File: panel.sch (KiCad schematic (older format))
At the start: 31 parts, among them J201 AudioJack2, J202 AudioJack2, J203 AudioJack2, J204 Conn_01x14, J205 AudioJack2, J206 AudioJack2, J207 Conn_01x09, J208 AudioJack2, J209 AudioJack2, J210 AudioJack2, SW201 SR1712F-0204-20F0A-N9-N-027, U201 TL072

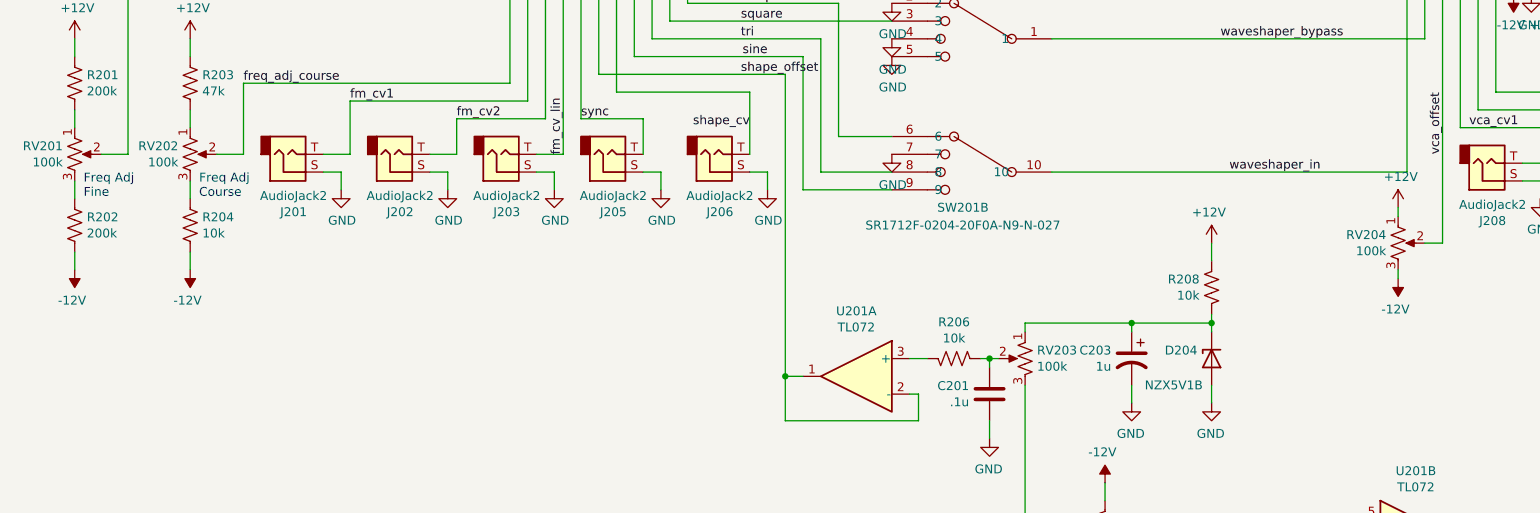
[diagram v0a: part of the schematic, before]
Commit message: Updated for tayda pots A-5513 and jacks A-2563
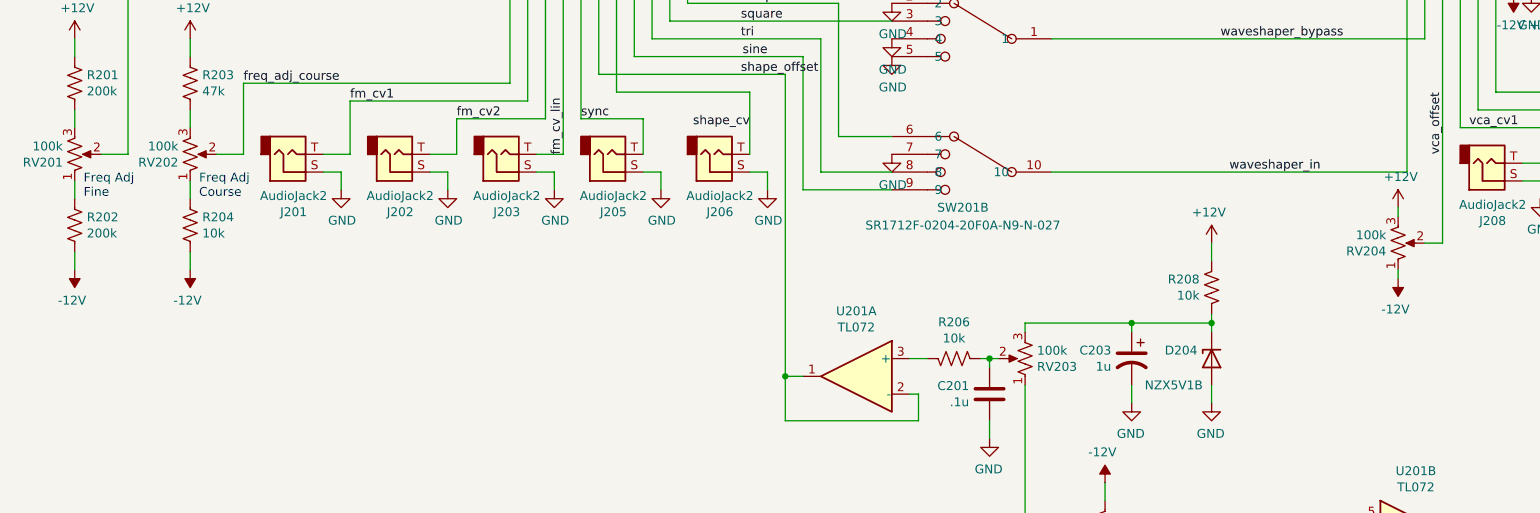
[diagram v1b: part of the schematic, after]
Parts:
- J201, J202, J203, J205, J206, J208, J209, J210: footprint ACJM-MV35:ACJM-MV35 -> A-2563:A-2563
- RV201, RV202, RV203, RV204: footprint Potentiometer_THT:Potentiometer_Bourns_PTV09A-1_Single_Vertical -> A-5513:A-5513
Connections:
- net +12V: now also RV204.3; no longer RV204.1
- net -12V: now also RV204.1; no longer RV204.3
- net at RV201.1: now also R202.1; no longer R201.2
- net at RV201.3: now also R201.2; no longer R202.1
- net at RV202.1: now also R204.1; no longer R203.2
- net at RV202.3: now also R203.2; no longer R204.1
- net at C203.1, D204.1 (K), R208.1: now also RV203.3; no longer RV203.1
- net at C202.2, D203.2 (A), R207.1: now also RV203.1; no longer RV203.3
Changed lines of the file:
@@
 F 0 "RV204" H 8283 3996 50  0000 R CNN
 F 1 "100k" H 8283 3905 50  0000 R CNN
-F 2 "Potentiometer_THT:Potentiometer_Bourns_PTV09A-1_Single_Vertical" H 8350 3950 50  0001 C CNN
+F 2 "A-5513:A-5513" H 8350 3950 50  0001 C CNN
 F 3 "~" H 8350 3950 50  0001 C CNN
 	1    8350 3950
-	1    0    0    -1
+	1    0    0    1
 $EndComp
 Wire Wire Line
@@
 F 0 "RV201" H 833 3496 50  0000 R CNN
 F 1 "100k" H 833 3405 50  0000 R CNN
-F 2 "Potentiometer_THT:Potentiometer_Bourns_PTV09A-1_Single_Vertical" H 900 3450 50  0001 C CNN
+F 2 "A-5513:A-5513" H 900 3450 50  0001 C CNN
 F 3 "~" H 900 3450 50  0001 C CNN
 	1    900  3450
-	1    0    0    -1
+	1    0    0    1
 $EndComp
 $Comp
@@
 F 0 "RV202" H 1483 3496 50  0000 R CNN
 F 1 "100k" H 1483 3405 50  0000 R CNN
-F 2 "Potentiometer_THT:Potentiometer_Bourns_PTV09A-1_Single_Vertical" H 1550 3450 50  0001 C CNN
+F 2 "A-5513:A-5513" H 1550 3450 50  0001 C CNN
 F 3 "~" H 1550 3450 50  0001 C CNN
 	1    1550 3450
-	1    0    0    -1
+	1    0    0    1
 $EndComp
 $Comp
@@
 F 0 "J201" H 2132 3775 50  0000 C CNN
 F 1 "AudioJack2" H 2132 3684 50  0000 C CNN
-F 2 "ACJM-MV35:ACJM-MV35" H 2100 3450 50  0001 C CNN
+F 2 "A-2563:A-2563" H 2100 3450 50  0001 C CNN
 F 3 "~" H 2100 3450 50  0001 C CNN
 	1    2100 3450
@@
 F 0 "J202" H 2732 3775 50  0000 C CNN
 F 1 "AudioJack2" H 2732 3684 50  0000 C CNN
-F 2 "ACJM-MV35:ACJM-MV35" H 2700 3450 50  0001 C CNN
+F 2 "A-2563:A-2563" H 2700 3450 50  0001 C CNN
 F 3 "~" H 2700 3450 50  0001 C CNN
 	1    2700 3450
@@
 F 0 "J203" H 3332 3775 50  0000 C CNN
 F 1 "AudioJack2" H 3332 3684 50  0000 C CNN
-F 2 "ACJM-MV35:ACJM-MV35" H 3300 3450 50  0001 C CNN
+F 2 "A-2563:A-2563" H 3300 3450 50  0001 C CNN
 F 3 "~" H 3300 3450 50  0001 C CNN
 	1    3300 3450
@@
 F 0 "J205" H 3932 3775 50  0000 C CNN
 F 1 "AudioJack2" H 3932 3684 50  0000 C CNN
-F 2 "ACJM-MV35:ACJM-MV35" H 3900 3450 50  0001 C CNN
+F 2 "A-2563:A-2563" H 3900 3450 50  0001 C CNN
 F 3 "~" H 3900 3450 50  0001 C CNN
 	1    3900 3450
@@
 F 0 "J206" H 4532 3775 50  0000 C CNN
 F 1 "AudioJack2" H 4532 3684 50  0000 C CNN
-F 2 "ACJM-MV35:ACJM-MV35" H 4500 3450 50  0001 C CNN
+F 2 "A-2563:A-2563" H 4500 3450 50  0001 C CNN
 F 3 "~" H 4500 3450 50  0001 C CNN
 	1    4500 3450
@@
 F 0 "RV203" H 6183 4646 50  0000 R CNN
 F 1 "100k" H 6183 4555 50  0000 R CNN
-F 2 "Potentiometer_THT:Potentiometer_Bourns_PTV09A-1_Single_Vertical" H 6250 4600 50  0001 C CNN
+F 2 "A-5513:A-5513" H 6250 4600 50  0001 C CNN
 F 3 "~" H 6250 4600 50  0001 C CNN
 	1    6250 4600
-	-1   0    0    -1
+	-1   0    0    1
 $EndComp
 $Comp
@@
 F 0 "J208" H 8882 3825 50  0000 C CNN
 F 1 "AudioJack2" H 8882 3734 50  0000 C CNN
-F 2 "ACJM-MV35:ACJM-MV35" H 8850 3500 50  0001 C CNN
+F 2 "A-2563:A-2563" H 8850 3500 50  0001 C CNN
 F 3 "~" H 8850 3500 50  0001 C CNN
 	1    8850 3500
@@
 F 0 "J209" H 9532 3825 50  0000 C CNN
 F 1 "AudioJack2" H 9532 3734 50  0000 C CNN
-F 2 "ACJM-MV35:ACJM-MV35" H 9500 3500 50  0001 C CNN
+F 2 "A-2563:A-2563" H 9500 3500 50  0001 C CNN
 F 3 "~" H 9500 3500 50  0001 C CNN
 	1    9500 3500
@@
 F 0 "J210" H 10182 3825 50  0000 C CNN
 F 1 "AudioJack2" H 10182 3734 50  0000 C CNN
-F 2 "ACJM-MV35:ACJM-MV35" H 10150 3500 50  0001 C CNN
+F 2 "A-2563:A-2563" H 10150 3500 50  0001 C CNN
 F 3 "~" H 10150 3500 50  0001 C CNN
 	1    10150 3500
@@
 $EndComp
 $Comp
-L power:+12V #PWR?
+L power:+12V #PWR0101
 U 1 1 606CEB9B
 P 4550 2000
-F 0 "#PWR?" H 4550 1850 50  0001 C CNN
+F 0 "#PWR0101" H 4550 1850 50  0001 C CNN
 F 1 "+12V" H 4565 2173 50  0000 C CNN
 F 2 "" H 4550 2000 50  0001 C CNN

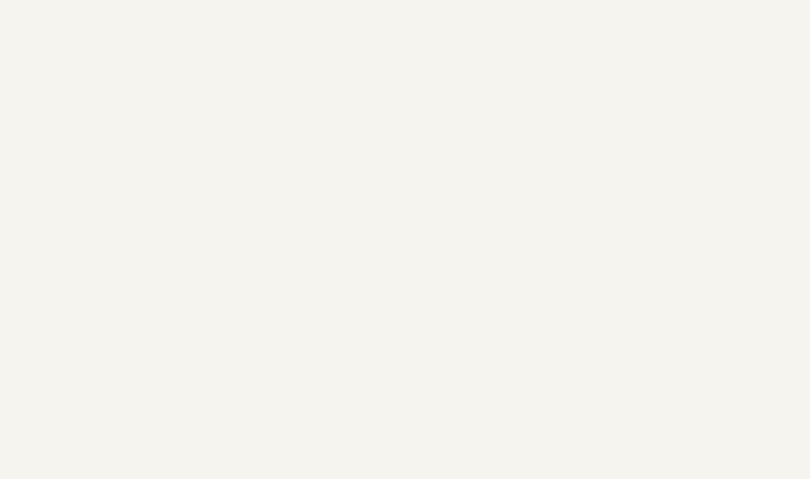
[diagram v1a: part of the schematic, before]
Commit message: Fixed op amp issue
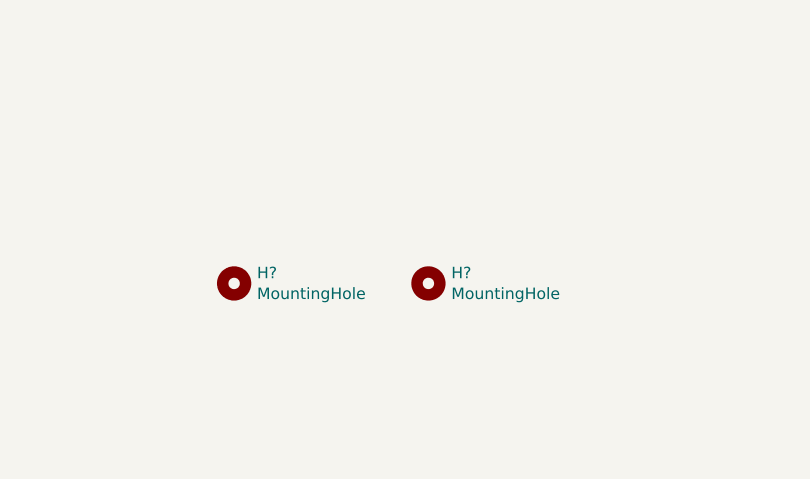
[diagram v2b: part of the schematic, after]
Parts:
- added H? (x2): MountingHole, MountingHole:MountingHole_3mm_Pad, symbol Mechanical:MountingHole
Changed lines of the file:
@@
 	-1   0    0    1
 $EndComp
+$Comp
+L Mechanical:MountingHole H?
+U 1 1 60AEEC78
+P 2750 5650
+F 0 "H?" H 2850 5696 50  0000 L CNN
+F 1 "MountingHole" H 2850 5605 50  0000 L CNN
+F 2 "MountingHole:MountingHole_3mm_Pad" H 2750 5650 50  0001 C CNN
+F 3 "~" H 2750 5650 50  0001 C CNN
+	1    2750 5650
+	1    0    0    -1
+$EndComp
+$Comp
+L Mechanical:MountingHole H?
+U 1 1 60AF2FA6
+P 1900 5650
+F 0 "H?" H 2000 5696 50  0000 L CNN
+F 1 "MountingHole" H 2000 5605 50  0000 L CNN
+F 2 "MountingHole:MountingHole_3mm_Pad" H 1900 5650 50  0001 C CNN
+F 3 "~" H 1900 5650 50  0001 C CNN
+	1    1900 5650
+	1    0    0    -1
+$EndComp
 $EndSCHEMATC
